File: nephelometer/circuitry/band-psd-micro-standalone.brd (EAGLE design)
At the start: 88 x 49 mm, 64 parts, among them IC1 LMC6484P, IC2 LM555N, IC3 74HCT74N, IC4 4044N, T1 2N2222, T2 2N2222, U1 MAX4544, U4 MotA

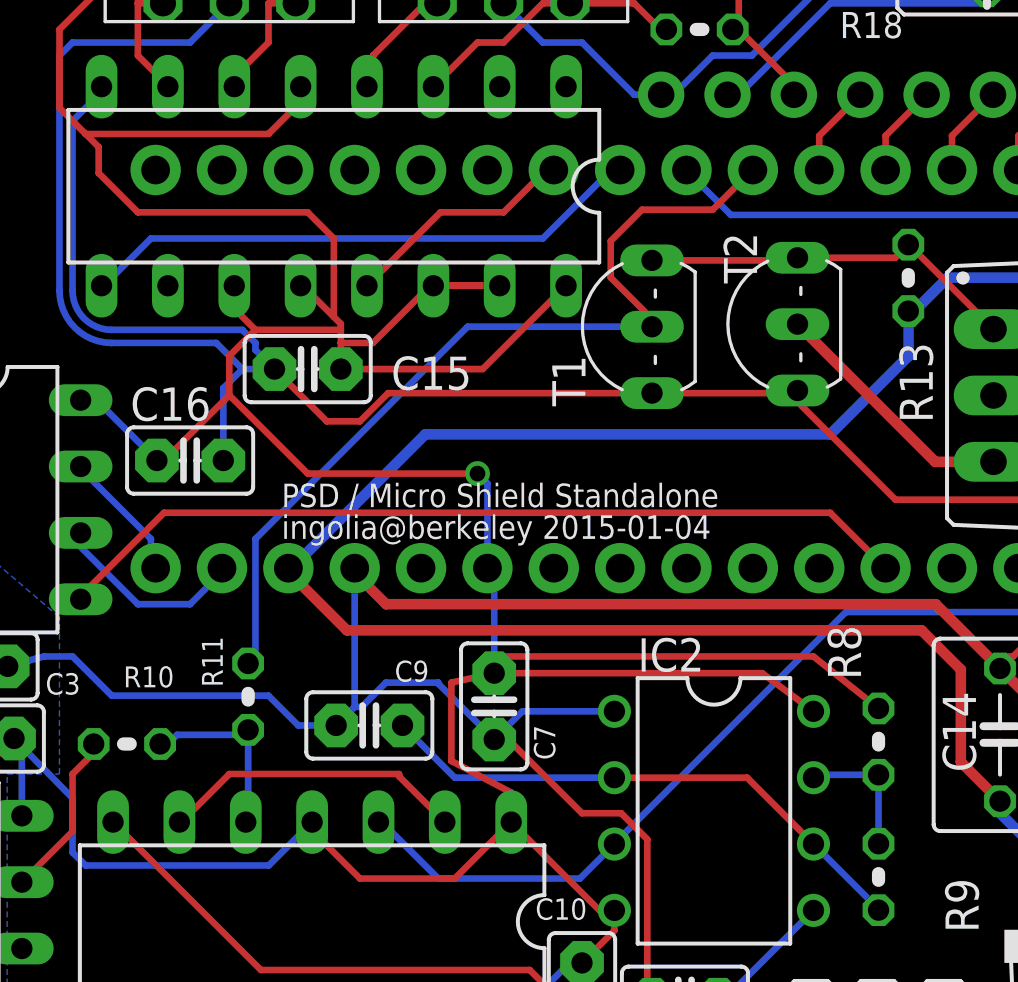
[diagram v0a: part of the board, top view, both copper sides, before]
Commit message: Fixed a minor flaw in which Arduino input pin is connected on the wrong side of the base resistor of the LED control and so never reads positive
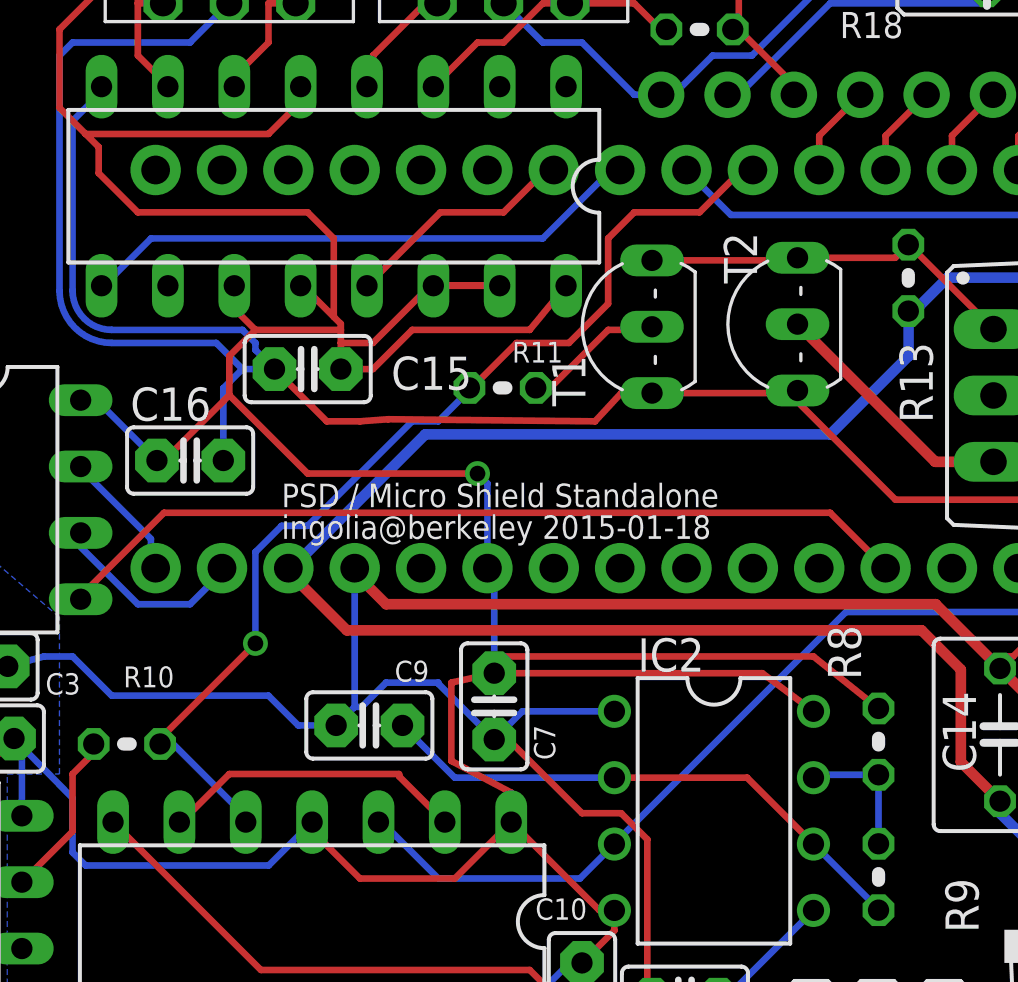
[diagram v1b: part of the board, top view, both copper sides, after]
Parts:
- moved R11 15.3 mm to (52.5, 32.3), turned to 0 degrees
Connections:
- net 5KHZ: now also U3.P$8
- net LEDCTRL: no longer U3.P$8
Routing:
- net 5KHZ: track 7.16 -> 40.9 mm, vias 0 -> 1
- net LEDCTRL: track 34.4 -> 5.64 mm
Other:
- board text added: "PSD / Micro Shield Standalone ingolia@berkeley 2015-01-18"
- board text removed: "PSD / Micro Shield Standalone ingolia@berkeley 2015-01-04"
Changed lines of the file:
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@@
 <?xml version="1.0" encoding="utf-8"?>
 <!DOCTYPE eagle SYSTEM "eagle.dtd">
-<eagle version="7.1.0">
+<eagle version="7.0.0">
 <drawing>
 <settings>
@@
 <wire x1="0" y1="35" x2="0" y2="6" width="0" layer="20"/>
 <text x="44" y="26.5" size="0.9" layer="21" distance="35">PSD / Micro Shield Standalone
-ingolia@berkeley 2015-01-04</text>
+ingolia@berkeley 2015-01-18</text>
 <polygon width="0.4064" layer="39">
 <vertex x="6.5" y="35"/>
@@
 <attribute name="VALUE" x="37.9464" y="19.8386" size="0.8" layer="27" ratio="12"/>
 </element>
-<element name="R11" library="adafruit" package="0204V" value="4K7" x="42.72" y="20.46" smashed="yes" rot="R90">
-<attribute name="NAME" x="41.7516" y="20.8264" size="0.8" layer="25" ratio="12" rot="R90"/>
-<attribute name="VALUE" x="41.8314" y="18.3264" size="0.8" layer="27" ratio="12" rot="R90"/>
+<element name="R11" library="adafruit" package="0204V" value="4K7" x="52.46" y="32.28" smashed="yes">
+<attribute name="NAME" x="52.8264" y="33.2484" size="0.8" layer="25" ratio="12"/>
+<attribute name="VALUE" x="50.3264" y="33.1686" size="0.8" layer="27" ratio="12"/>
 </element>
 <element name="T1" library="adafruit" package="TO92-EBC-OVAL" value="2N2222" x="56.91" y="34.62" smashed="yes" rot="R90">
@@
 <contactref element="R21" pad="2"/>
 <wire x1="63.61" y1="43.5" x2="63.5" y2="43.5" width="0.254" layer="16"/>
-<wire x1="46.27" y1="33" x2="51.7" y2="33" width="0.254" layer="1"/>
-<wire x1="51.7" y1="33" x2="54.89" y2="36.19" width="0.254" layer="1"/>
+<wire x1="46.27" y1="33" x2="47.5" y2="33" width="0.254" layer="1"/>
+<wire x1="47.5" y1="33" x2="49" y2="34.5" width="0.254" layer="1"/>
+<wire x1="49" y1="34.5" x2="53.5" y2="34.5" width="0.254" layer="1"/>
+<wire x1="53.5" y1="34.5" x2="54.89" y2="36.19" width="0.254" layer="1"/>
 <wire x1="46.27" y1="33" x2="46.27" y2="34" width="0.254" layer="1"/>
 <wire x1="46.27" y1="34" x2="46.27" y2="34.5" width="0.254" layer="1"/>
@@
 <wire x1="86.47" y1="43.5" x2="86.47" y2="38.22" width="0.4064" layer="1"/>
 <wire x1="86.47" y1="38.22" x2="80.76" y2="32.51" width="0.4064" layer="1"/>
-<wire x1="58.18" y1="32.08" x2="48.08" y2="32.08" width="0.254" layer="1"/>
-<wire x1="48.08" y1="32.08" x2="47" y2="31" width="0.254" layer="1"/>
+<wire x1="58.18" y1="32.08" x2="57" y2="32.08" width="0.254" layer="1"/>
+<wire x1="57" y1="32.08" x2="56" y2="31" width="0.254" layer="1"/>
+<wire x1="56" y1="31" x2="48.08" y2="31.08" width="0.254" layer="1"/>
+<wire x1="48.08" y1="31.08" x2="47" y2="31" width="0.254" layer="1"/>
 <wire x1="47" y1="31" x2="45.73" y2="31" width="0.254" layer="1"/>
 <wire x1="45.73" y1="31" x2="43.73" y2="33" width="0.254" layer="1"/>
@@
 <contactref element="R11" pad="2"/>
 <contactref element="T1" pad="B"/>
-<wire x1="42.72" y1="21.73" x2="43" y2="22.01" width="0.254" layer="16"/>
-<wire x1="43" y1="22.01" x2="43" y2="26.5" width="0.254" layer="16"/>
-<wire x1="43" y1="26.5" x2="51.12" y2="34.62" width="0.254" layer="16"/>
-<wire x1="51.12" y1="34.62" x2="58.18" y2="34.62" width="0.254" layer="16"/>
-<contactref element="U3" pad="P$8"/>
-<wire x1="58.5" y1="35" x2="58.18" y2="34.62" width="0.254" layer="16"/>
-<wire x1="57.8" y1="39.1" x2="56.6" y2="37.9" width="0.254" layer="1"/>
-<wire x1="60.5" y1="39.1" x2="57.8" y2="39.1" width="0.254" layer="1"/>
-<wire x1="62" y1="40.6" x2="60.5" y2="39.1" width="0.254" layer="1"/>
-<wire x1="62" y1="40.6" x2="62.04" y2="40.62" width="0.254" layer="1"/>
-<wire x1="58.1" y1="35" x2="58.1" y2="34.7" width="0.254" layer="1"/>
-<wire x1="56.6" y1="36.5" x2="58.1" y2="35" width="0.254" layer="1"/>
-<wire x1="56.6" y1="37.9" x2="56.6" y2="36.5" width="0.254" layer="1"/>
-<wire x1="58.1" y1="34.7" x2="58.18" y2="34.62" width="0.254" layer="1"/>
+<wire x1="56.5" y1="34.5" x2="58" y2="34.5" width="0.254" layer="1"/>
+<wire x1="54" y1="32" x2="56.5" y2="34.5" width="0.254" layer="1"/>
+<wire x1="58" y1="34.5" x2="58.18" y2="34.62" width="0.254" layer="1"/>
+<wire x1="54" y1="32" x2="53.73" y2="32.28" width="0.254" layer="1"/>
 </signal>
 <signal name="N$23">
@@
 <contactref element="R10" pad="2"/>
 <contactref element="IC3" pad="5"/>
-<wire x1="42.63" y1="15.66" x2="42.72" y2="15.75" width="0.254" layer="16"/>
-<wire x1="42.72" y1="15.75" x2="42.72" y2="19.19" width="0.254" layer="16"/>
-<wire x1="42.72" y1="19.19" x2="42.53" y2="19" width="0.254" layer="16"/>
-<wire x1="42.53" y1="19" x2="40" y2="19" width="0.254" layer="16"/>
-<wire x1="40" y1="19" x2="39.65" y2="18.65" width="0.254" layer="16"/>
-<wire x1="39.65" y1="18.65" x2="39.35" y2="18.65" width="0.254" layer="16"/>
+<contactref element="U3" pad="P$8"/>
+<wire x1="39.5" y1="19" x2="42.5" y2="16" width="0.254" layer="16"/>
+<wire x1="42.5" y1="16" x2="42.63" y2="15.66" width="0.254" layer="16"/>
+<wire x1="39.5" y1="19" x2="39.35" y2="18.65" width="0.254" layer="16"/>
+<wire x1="57.5" y1="39" x2="56.5" y2="38" width="0.254" layer="1"/>
+<wire x1="60" y1="39" x2="57.5" y2="39" width="0.254" layer="1"/>
+<wire x1="62" y1="41" x2="60" y2="39" width="0.254" layer="1"/>
+<wire x1="62" y1="41" x2="62.04" y2="40.62" width="0.254" layer="1"/>
+<wire x1="53" y1="34" x2="51.5" y2="32.5" width="0.254" layer="1"/>
+<wire x1="55" y1="34" x2="53" y2="34" width="0.254" layer="1"/>
+<wire x1="56.5" y1="35.5" x2="55" y2="34" width="0.254" layer="1"/>
+<wire x1="56.5" y1="38" x2="56.5" y2="35.5" width="0.254" layer="1"/>
+<wire x1="51.5" y1="32.5" x2="51.19" y2="32.28" width="0.254" layer="1"/>
+<wire x1="50" y1="31" x2="51" y2="32" width="0.254" layer="16"/>
+<wire x1="49" y1="31" x2="50" y2="31" width="0.254" layer="16"/>
+<wire x1="45" y1="27" x2="49" y2="31" width="0.254" layer="16"/>
+<wire x1="44" y1="27" x2="45" y2="27" width="0.254" layer="16"/>
+<wire x1="43" y1="26" x2="44" y2="27" width="0.254" layer="16"/>
+<wire x1="43" y1="22.5" x2="43" y2="26" width="0.254" layer="16"/>
+<wire x1="39.5" y1="19" x2="43" y2="22.5" width="0.254" layer="1"/>
+<wire x1="51" y1="32" x2="51.19" y2="32.28" width="0.254" layer="16"/>
+<wire x1="39.5" y1="19" x2="39.35" y2="18.65" width="0.254" layer="1"/>
+<via x="43" y="22.5" extent="1-16" drill="0.6"/>
 </signal>
 <signal name="N$12">

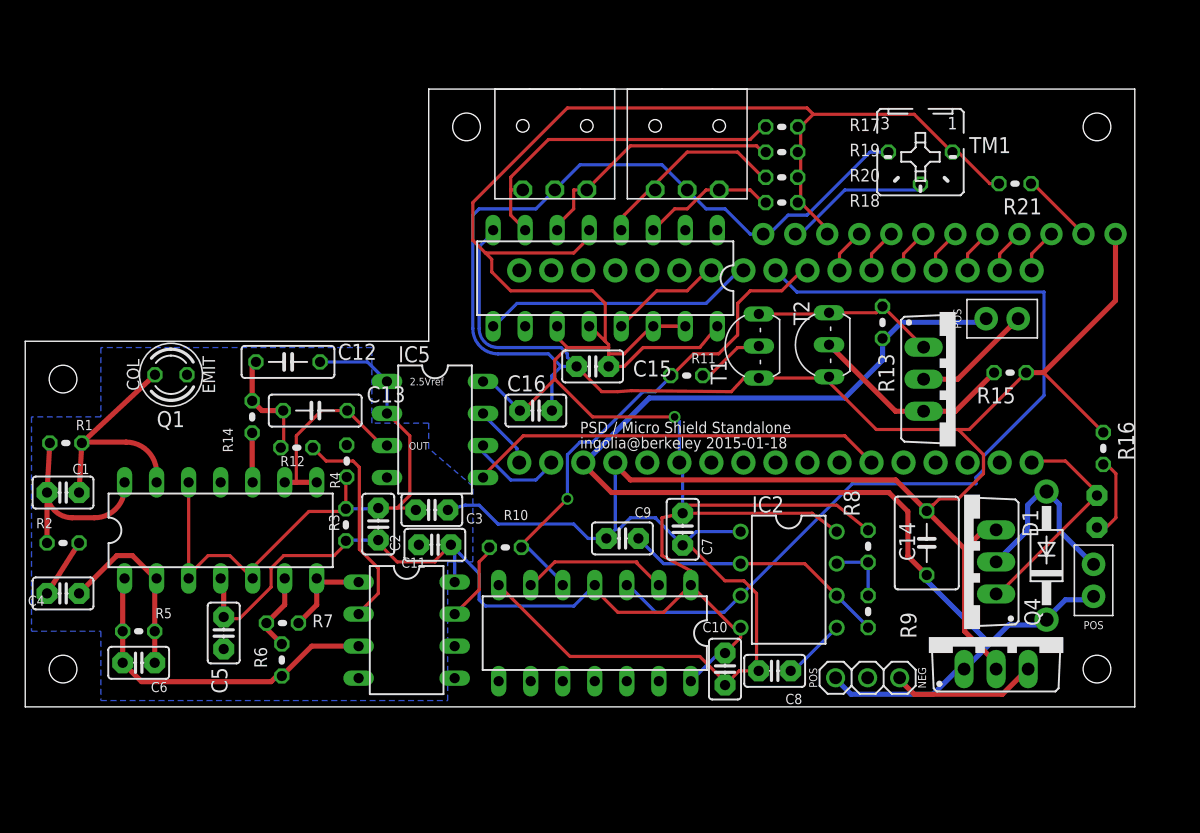
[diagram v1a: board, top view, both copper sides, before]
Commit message: Enlarged board, included 5V regulator on board, more decoupling, 4 buttons on 4 PCIO pins
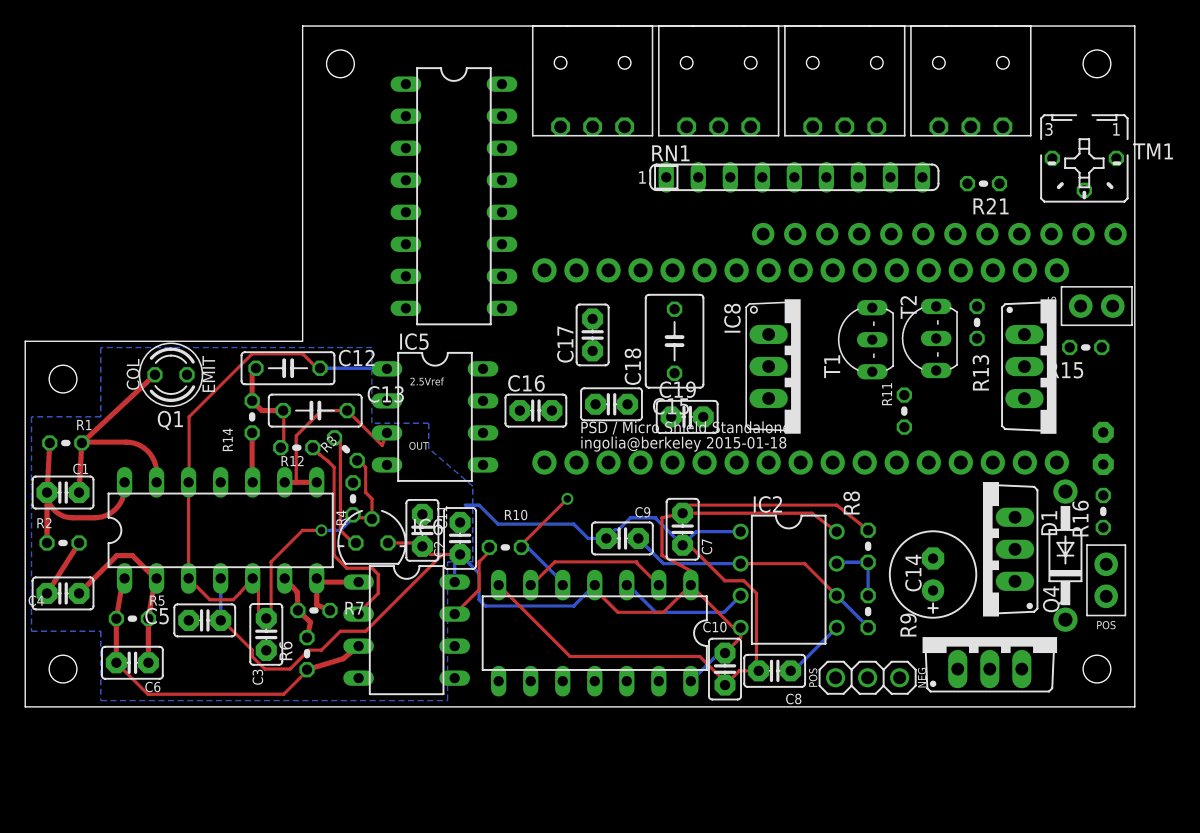
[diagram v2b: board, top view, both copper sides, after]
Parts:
- removed R17, R18, R19, R20: 10K, adafruit:0204V
- added C17, C19: 0.33µ, adafruit:C025-025X050
- added C18: 22µ, adafruit:C050-045X075
- added IC6: (no value), v-reg:317L
- added IC8: 7805TV, linear:TO220V
- added RN1: (no value), resistor-sil:SIL9
- added U$8, U$9: (no value), ingolia:APE1F-5M-10Z
- C14: value 10u -> 100µ; device adafruit:C050-050X075 -> adafruit:E2,5-7
- C3: value 100n -> 1u
- C4: value 20n -> 100n
- C6: value 50p -> 10p
- R2: value 10K -> 1K5
- R5: value 100K -> 470K
- moved U$5 23.5 mm to (65.0, 52.0)
- moved U$6 23.0 mm to (75.0, 52.0)
- moved R11 17.5 mm to (69.7, 29.5), turned to 90 degrees
- moved C3 16.4 mm to (19.1, 11.8), turned to 270 degrees
- moved IC4 13.6 mm to (34.0, 46.5), turned to 270 degrees
- moved TM1 13.0 mm to (84.0, 49.5)
- moved U$7 11.2 mm to (25.0, 57.0)
- moved T1 9.01 mm to (65.9, 35.1)
- moved T2 8.51 mm to (71.0, 35.2)
- moved Q2 8.06 mm to (79.2, 33.0)
- moved JP1 7.57 mm to (82.4, 36.5)
- moved R13 7.50 mm to (75.5, 36.5)
- moved R15 6.32 mm to (84.1, 34.5)
- moved R3 6.00 mm to (25.4, 26.4), turned to 315 degrees
- moved LED1 5.02 mm to (85.5, 26.5)
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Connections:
- new net N$35: IC6.1, R3.1
- new net N$39: IC4.1, U3.P$15
- new net N$40: IC4.6, RN1.7, U$5.P$1
- new net N$42: IC4.3, RN1.8, U$6.P$3
- new net N$43: IC4.4, RN1.9, U$6.P$1
- new net N$44: IC4.7, RN1.6, U$5.P$3
- new net N$45: IC4.10, U3.P$14
- net +12V: now also C14.+, C17.1, IC8.1; no longer C14.1, U3.P$20
- net +5V: now also C18.1, C19.1, IC6.3, IC8.3, RN1.1; no longer IC4.11, IC4.12, IC4.14, IC4.15, R17.2, R18.2, R19.2, R20.2, R3.2, U3.P$23
- net 10KHZ: now also U3.P$28; no longer U3.P$9
- net 2.5V: now also IC6.2, R3.2; no longer C2.1, R3.1
- net 5KHZ: now also U3.P$27; no longer U3.P$8
- net CS_ADC: now also U3.P$26; no longer U3.P$29
- net GND: now also C14.-, C17.2, C18.2, C19.2, C2.1, U$8.P$2, U$9.P$2; no longer C14.2
- net N$31: now also IC4.13; no longer IC4.9
- net N$32: now also IC4.9; no longer IC4.13
- net N$33: now also IC4.15, RN1.2, U$9.P$3; no longer IC4.7, R17.1, U$5.P$1
- net N$34: now also IC4.14, RN1.3, U$9.P$1; no longer IC4.6, R19.1, U$5.P$3
- net N$36: now also IC4.11, RN1.4, U$8.P$3; no longer IC4.3, R18.1, U$6.P$3
- net N$37: now also IC4.12, RN1.5, U$8.P$1; no longer IC4.4, R20.1, U$6.P$1
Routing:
- net GND: track 266.3 -> 63.4 mm
- net +5V: track 248.8 -> 107.4 mm, vias 1 -> 0
- net +12V: track 102.9 -> 0.00 mm
- net 10KHZ: track 72.3 -> 10.6 mm
- net CS_ADC: track 33.1 -> 0.00 mm
- net 5KHZ: track 40.9 -> 10.3 mm
- net N$33: track 27.5 -> 0.00 mm
- net N$31: track 21.6 -> 0.00 mm
- net N$34: track 20.8 -> 0.00 mm
- net N$19: track 17.7 -> 0.00 mm
- net N$14: track 16.5 -> 0.00 mm
- net N$37: track 15.9 -> 0.00 mm
- net N$3: track 15.1 -> 0.00 mm
- net N$8: track 14.7 -> 0.00 mm
- net N$38: track 11.8 -> 0.00 mm
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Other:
- board size 88 x 49 mm -> 88 x 54 mm

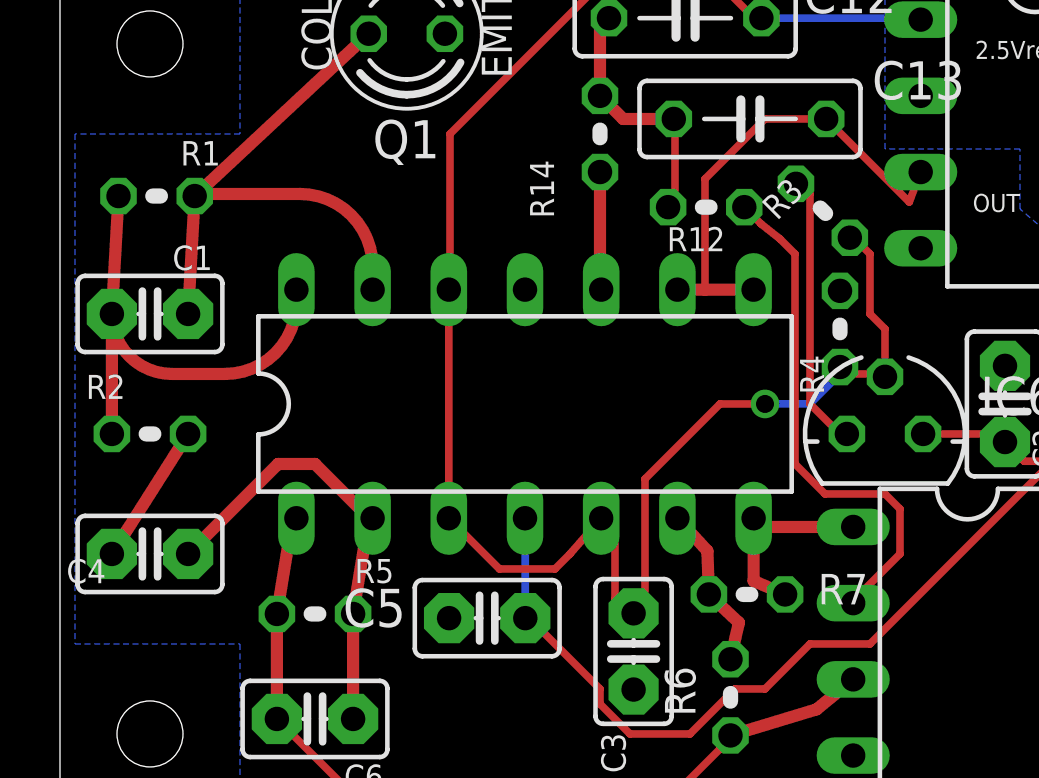
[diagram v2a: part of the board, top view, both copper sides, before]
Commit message: Fixed up filter design -- topology of high-gain bandpass and component values for low-pass
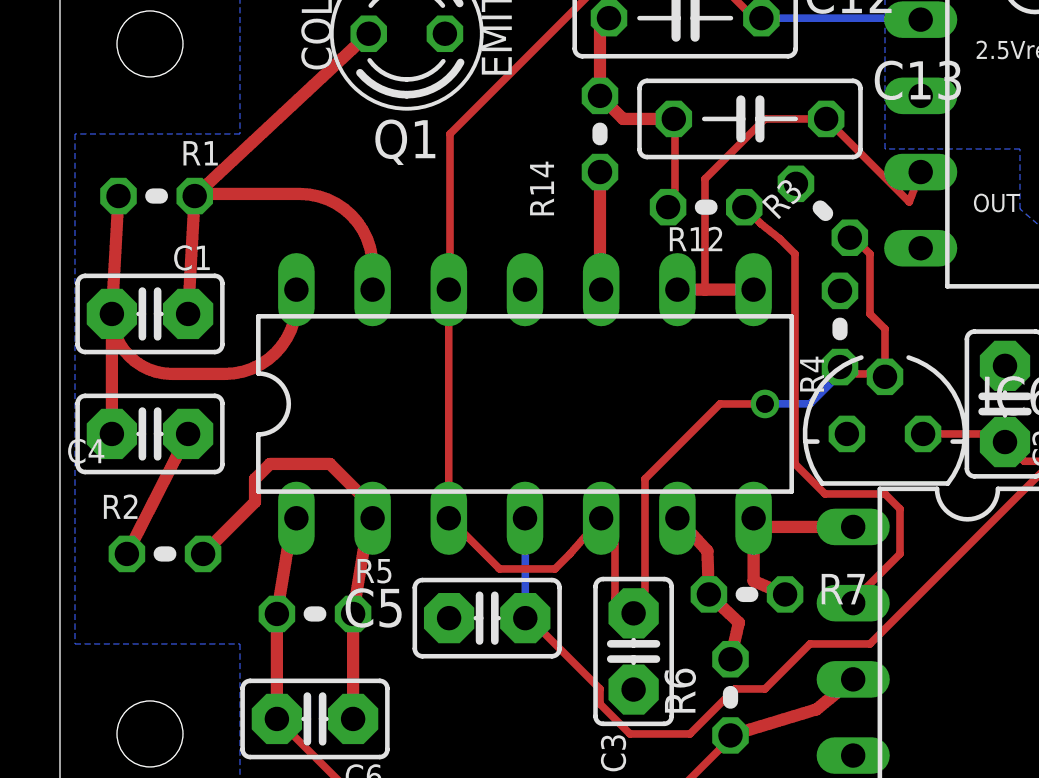
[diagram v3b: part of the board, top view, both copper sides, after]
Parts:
- C12: value 10u -> 22nF
- C13: value 10u -> 50nF
- R12: value 1K0 -> 330K
- R14: value 1K0 -> 680K
- R2: value 1K5 -> 1K0
- R5: value 470K -> 330K
- moved R2 4.03 mm to (3.50, 15.0)
- moved C4 4.00 mm to (3.00, 19.0)
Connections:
- removed net N$11: 16X2.4, U3.P$7
- removed net N$15: 16X2.5, U3.P$6
- removed net N$20: 16X2.6, U3.P$5
- removed net N$21: 16X2.7, U3.P$4
- removed net N$24: 16X2.8, U3.P$3
- removed net N$29: 16X2.9, U3.P$2
- removed net N$30: 16X2.10, U3.P$1
- net 2.5V: now also R3.1; no longer R3.2, R4.2
- net N$2: now also C4.2, R2.1; no longer C4.1, R2.2
- net N$22: now also C4.1; no longer R2.1
- net N$25: now also R2.2; no longer C4.2
- net N$35: now also R3.2, R4.2; no longer R3.1
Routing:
- net N$35: track 9.22 -> 0.00 mm
- net 2.5V: track 60.1 -> 59.5 mm
